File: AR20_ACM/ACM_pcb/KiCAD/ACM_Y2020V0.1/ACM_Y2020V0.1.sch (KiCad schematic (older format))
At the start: 2 parts, among them J1 TC2030-MCP-NL, U1 ATmega328PB-AU

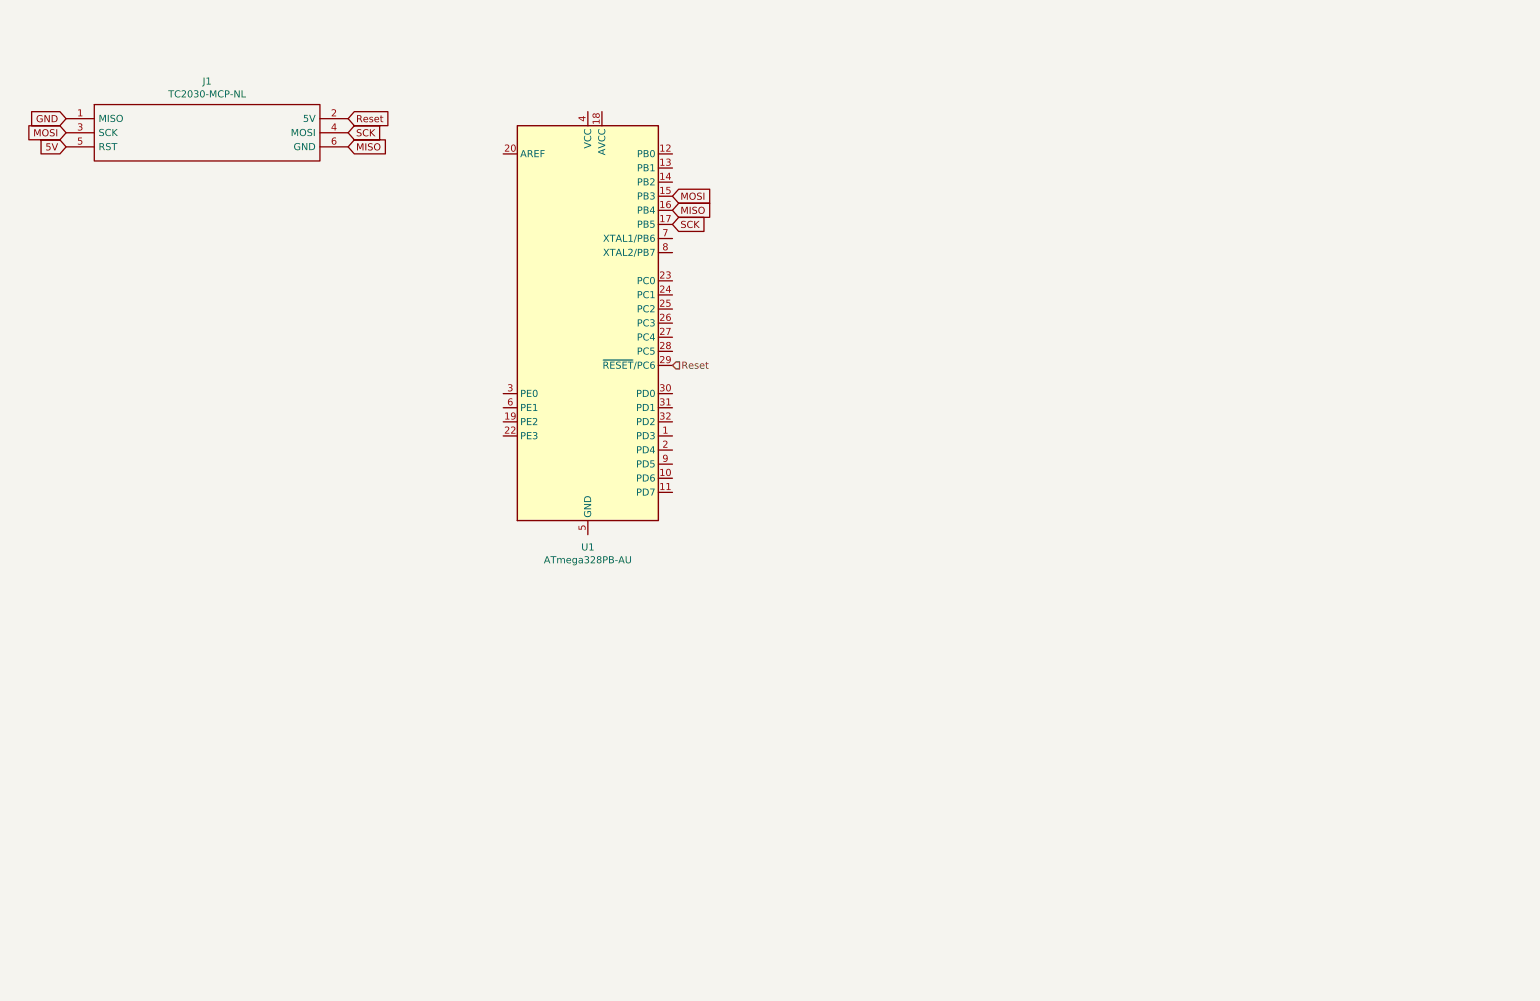
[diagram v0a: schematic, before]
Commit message: Added MCP25625 and PDFS
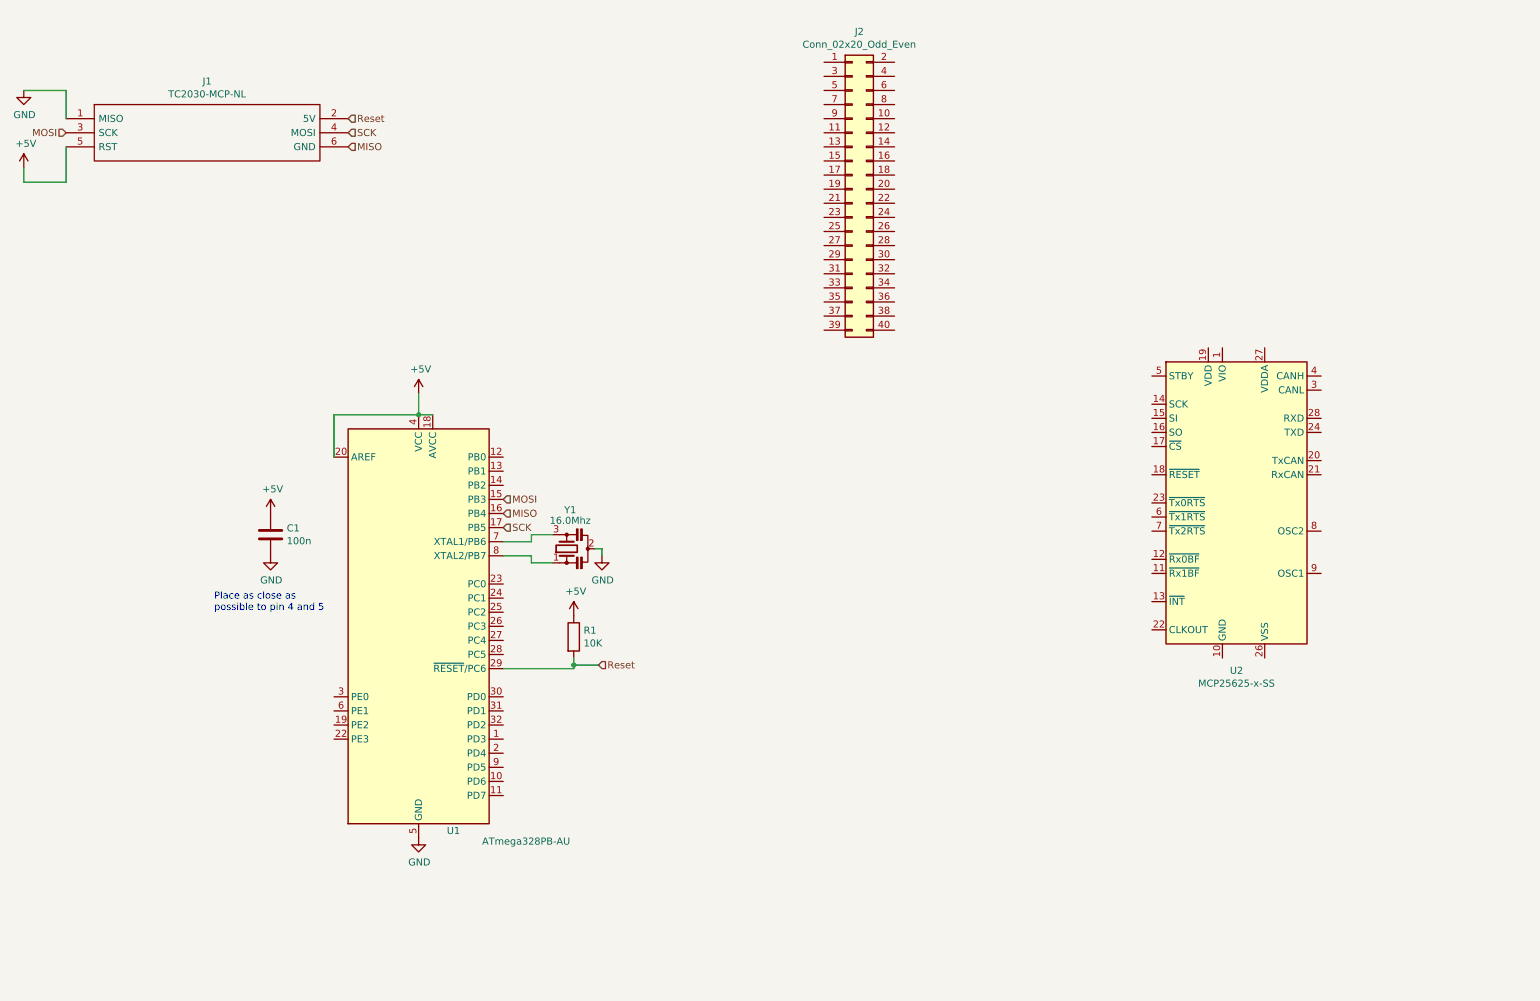
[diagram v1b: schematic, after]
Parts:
- added C1: 100n, Capacitor_SMD:C_0402_1005Metric, symbol Device:C
- added J2: Conn_02x20_Odd_Even, Connector_PinSocket_1.00mm:PinSocket_2x20_P1.00mm_Vertical_SMD, symbol Connector_Generic:Conn_02x20_Odd_Even
- added R1: 10K, Resistor_SMD:R_0402_1005Metric, symbol Device:R
- added U2: MCP25625-x-SS, Package_DFN_QFN:QFN-28-1EP_6x6mm_P0.65mm_EP4.8x4.8mm, symbol Interface_CAN_LIN:MCP25625-x-SS
- added Y1: 16.0Mhz, CSTNE16M0V530000R0:CSTNE16M0V530000R0, symbol Device:Resonator_Small
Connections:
- net 5V is gone; now on net +5V: J1.5 (RST)
- net GND: now also U1.21 (GND), U1.5 (GND), C1.2, Y1.2
- net Reset: now also R1.2
- net +5V: now reaches U1.18 (AVCC)
- net +5V: now also U1.20 (AREF), U1.4 (VCC), C1.1, R1.1
- net at U1.7 (XTAL1/PB6): now also Y1.3
- net at U1.8 (XTAL2/PB7): now also Y1.1
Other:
- note added: "Place as close as \npossible to pin 4 and 5"
- moved on the sheet: U1
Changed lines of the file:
@@
 EESchema Schematic File Version 4
+LIBS:ACM_Y2020V0.1-cache
 EELAYER 29 0
 EELAYER END
@@
 	1    0    0    -1
 $EndComp
+Text HLabel 3950 4250 2    50   Input ~ 0
+SCK
+Text HLabel 3950 4150 2    50   Input ~ 0
+MISO
+Text HLabel 3950 4050 2    50   Input ~ 0
+MOSI
+Text HLabel 850  1450 0    50   Input ~ 0
+MOSI
+Text HLabel 2850 1350 2    50   Input ~ 0
+Reset
+Text HLabel 2850 1450 2    50   Input ~ 0
+SCK
+Text HLabel 2850 1550 2    50   Input ~ 0
+MISO
+$Comp
+L power:GND #PWR0101
+U 1 1 5D3A6728
+P 550 1150
+F 0 "#PWR0101" H 550 900 50  0001 C CNN
+F 1 "GND" H 555 977 50  0000 C CNN
+F 2 "" H 550 1150 50  0001 C CNN
+F 3 "" H 550 1150 50  0001 C CNN
+	1    550  1150
+	1    0    0    -1
+$EndComp
+$Comp
+L power:GND #PWR0102
+U 1 1 5D3A8A7B
+P 3350 6450
+F 0 "#PWR0102" H 3350 6200 50  0001 C CNN
+F 1 "GND" H 3355 6277 50  0000 C CNN
+F 2 "" H 3350 6450 50  0001 C CNN
+F 3 "" H 3350 6450 50  0001 C CNN
+	1    3350 6450
+	1    0    0    -1
+$EndComp
+Wire Wire Line
+	850  1350 850  1150
+Wire Wire Line
+	850  1150 550  1150
+Wire Wire Line
+	850  1550 850  1800
+Wire Wire Line
+	850  1800 550  1800
+Wire Wire Line
+	550  1800 550  1700
+$Comp
+L power:+5V #PWR0103
+U 1 1 5D3A42C5
+P 550 1700
+F 0 "#PWR0103" H 550 1550 50  0001 C CNN
+F 1 "+5V" H 565 1873 50  0000 C CNN
+F 2 "" H 550 1700 50  0001 C CNN
+F 3 "" H 550 1700 50  0001 C CNN
+	1    550  1700
+	1    0    0    -1
+$EndComp
+$Comp
+L power:+5V #PWR0104
+U 1 1 5D3AF650
+P 3350 3300
+F 0 "#PWR0104" H 3350 3150 50  0001 C CNN
+F 1 "+5V" H 3365 3473 50  0000 C CNN
+F 2 "" H 3350 3300 50  0001 C CNN
+F 3 "" H 3350 3300 50  0001 C CNN
+	1    3350 3300
+	1    0    0    -1
+$EndComp
+Wire Wire Line
+	3450 3450 3350 3450
+Wire Wire Line
+	3350 3300 3350 3450
+Connection ~ 3350 3450
+Wire Wire Line
+	2750 3750 2750 3450
+Wire Wire Line
+	2750 3450 3350 3450
+$Comp
+L Device:C C1
+U 1 1 5D3B17F8
+P 2300 4300
+F 0 "C1" H 2415 4346 50  0000 L CNN
+F 1 "100n" H 2415 4255 50  0000 L CNN
+F 2 "Capacitor_SMD:C_0402_1005Metric" H 2338 4150 50  0001 C CNN
+F 3 "~" H 2300 4300 50  0001 C CNN
+	1    2300 4300
+	1    0    0    -1
+$EndComp
+$Comp
+L power:+5V #PWR0105
+U 1 1 5D3B309C
+P 2300 4150
+F 0 "#PWR0105" H 2300 4000 50  0001 C CNN
+F 1 "+5V" H 2315 4323 50  0000 C CNN
+F 2 "" H 2300 4150 50  0001 C CNN
+F 3 "" H 2300 4150 50  0001 C CNN
+	1    2300 4150
+	1    0    0    -1
+$EndComp
+$Comp
+L power:GND #PWR0106
+U 1 1 5D3B39A1
+P 2300 4450
+F 0 "#PWR0106" H 2300 4200 50  0001 C CNN
+F 1 "GND" H 2305 4277 50  0000 C CNN
+F 2 "" H 2300 4450 50  0001 C CNN
+F 3 "" H 2300 4450 50  0001 C CNN
+	1    2300 4450
+	1    0    0    -1
+$EndComp
+Text Notes 1900 4850 0    50   ~ 0
+Place as close as \npossible to pin 4 and 5
+$Comp
+L Device:Resonator_Small Y1
+U 1 1 5D3C125F
+P 4400 4400
+F 0 "Y1" V 4675 4375 50  0000 C CNN
+F 1 "16.0Mhz" V 4600 4375 50  0000 C CNN
+F 2 "CSTNE16M0V530000R0:CSTNE16M0V530000R0" H 4375 4400 50  0001 C CNN
+F 3 "~" H 4375 4400 50  0001 C CNN
+	1    4400 4400
+	0    -1   -1   0
+$EndComp
+$Comp
+L power:GND #PWR0107
+U 1 1 5D3C307D
+P 4650 4450
+F 0 "#PWR0107" H 4650 4200 50  0001 C CNN
+F 1 "GND" H 4655 4277 50  0000 C CNN
+F 2 "" H 4650 4450 50  0001 C CNN
+F 3 "" H 4650 4450 50  0001 C CNN
+	1    4650 4450
+	1    0    0    -1
+$EndComp
+Wire Wire Line
+	3950 4450 4150 4450
+Wire Wire Line
+	4150 4450 4150 4500
+Wire Wire Line
+	4150 4500 4300 4500
+Wire Wire Line
+	3950 4350 4150 4350
+Wire Wire Line
+	4150 4350 4150 4300
+Wire Wire Line
+	4150 4300 4300 4300
+Wire Wire Line
+	4600 4400 4650 4400
+Wire Wire Line
+	4650 4400 4650 4450
+$Comp
+L Device:R R1
+U 1 1 5D3CAE32
+P 4450 5025
+F 0 "R1" H 4520 5071 50  0000 L CNN
+F 1 "10K" H 4520 4980 50  0000 L CNN
+F 2 "Resistor_SMD:R_0402_1005Metric" V 4380 5025 50  0001 C CNN
+F 3 "~" H 4450 5025 50  0001 C CNN
+	1    4450 5025
+	1    0    0    -1
+$EndComp
+Wire Wire Line
+	3950 5250 4450 5250
+$Comp
+L power:+5V #PWR0108
+U 1 1 5D3CE356
+P 4450 4875
+F 0 "#PWR0108" H 4450 4725 50  0001 C CNN
+F 1 "+5V" H 4465 5048 50  0000 C CNN
+F 2 "" H 4450 4875 50  0001 C CNN
+F 3 "" H 4450 4875 50  0001 C CNN
+	1    4450 4875
+	1    0    0    -1
+$EndComp
+Connection ~ 4450 5225
+Wire Wire Line
+	4450 5225 4450 5175
+Wire Wire Line
+	4450 5250 4450 5225
+Wire Wire Line
+	4625 5225 4450 5225
+Text HLabel 4625 5225 2    50   Input ~ 0
+Reset
 $Comp
 L MCU_Microchip_ATmega:ATmega328PB-AU U1
 U 1 1 5D38D7A6
-P 4550 2800
-F 0 "U1" H 4550 1211 50  0000 C CNN
-F 1 "ATmega328PB-AU" H 4550 1120 50  0000 C CNN
-F 2 "Package_QFP:TQFP-32_7x7mm_P0.8mm" H 4550 2800 50  0001 C CIN
-F 3 "http://ww1.microchip.com/downloads/en/DeviceDoc/40001906C.pdf" H 4550 2800 50  0001 C CNN
-	1    4550 2800
-	1    0    0    -1
-$EndComp
-Text GLabel 2850 1350 2    50   Input ~ 0
-Reset
-Text GLabel 2850 1450 2    50   Input ~ 0
-SCK
-Text GLabel 2850 1550 2    50   Input ~ 0
-MISO
-Text GLabel 850  1350 0    50   Input ~ 0
-GND
-Text GLabel 850  1450 0    50   Input ~ 0
-MOSI
-Text GLabel 850  1550 0    50   Input ~ 0
-5V
-Text GLabel 5150 1900 2    50   Input ~ 0
-MOSI
-Text GLabel 5150 2000 2    50   Input ~ 0
-MISO
-Text GLabel 5150 2100 2    50   Input ~ 0
-SCK
-Text HLabel 5150 3100 2    50   Input ~ 0
-Reset
+P 3350 4950
+F 0 "U1" H 3550 3500 50  0000 L CNN
+F 1 "ATmega328PB-AU" H 3800 3425 50  0000 L CNN
+F 2 "Package_QFP:TQFP-32_7x7mm_P0.8mm" H 3350 4950 50  0001 C CIN
+F 3 "http://ww1.microchip.com/downloads/en/DeviceDoc/40001906C.pdf" H 3350 4950 50  0001 C CNN
+	1    3350 4950
+	1    0    0    -1
+$EndComp
+$Comp
+L Interface_CAN_LIN:MCP25625-x-SS U2
+U 1 1 5D3DCB03
+P 9150 4075
+F 0 "U2" H 9150 2886 50  0000 C CNN
+F 1 "MCP25625-x-SS" H 9150 2795 50  0000 C CNN
+F 2 "Package_DFN_QFN:QFN-28-1EP_6x6mm_P0.65mm_EP4.8x4.8mm" H 9250 3775 50  0001 C CNN
+F 3 "http://ww1.microchip.com/downloads/en/DeviceDoc/20005282B.pdf" H 9150 4675 50  0001 C CNN
+	1    9150 4075
+	1    0    0    -1
+$EndComp
+$Comp
+L Connector_Generic:Conn_02x20_Odd_Even J2
+U 1 1 5D3E347E
+P 6425 1850
+F 0 "J2" H 6475 2967 50  0000 C CNN
+F 1 "Conn_02x20_Odd_Even" H 6475 2876 50  0000 C CNN
+F 2 "Connector_PinSocket_1.00mm:PinSocket_2x20_P1.00mm_Vertical_SMD" H 6425 1850 50  0001 C CNN
+F 3 "~" H 6425 1850 50  0001 C CNN
+	1    6425 1850
+	1    0    0    -1
+$EndComp
 $EndSCHEMATC

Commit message: See change log for update.
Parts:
- added C2, C3, C4, C5: 0.1uF, Capacitor_SMD:C_0402_1005Metric, symbol Device:C
- added D1: 15V, Diode_SMD:D_SOD-323F, symbol Device:D_Zener
- added F1: 200mA, Fuse:Fuse_0603_1608Metric, symbol Device:Polyfuse_Small
- added R2: 120Ohm, Resistor_SMD:R_0603_1608Metric, symbol Device:R
- added R3: 10KOhm, Resistor_SMD:R_0402_1005Metric, symbol Device:R
- added U3: SPX3819M5-L-5-0, Package_TO_SOT_SMD:SOT-23-5, symbol Regulator_Linear:SPX3819M5-L-5-0
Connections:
- net labels added: +12V, CANH, CANL, CAN_CS, CAN_INT, CLK_MCP
- wire segments 21 -> 64
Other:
- note added: "CAN MCU"
- note added: "Close as possible to MCP-chip"
- note added: "Connector"
- note added: "ICSP"
- note added: "Main MCU"
- note added: "Power and protection circuits"
- moved on the sheet: C1, J1, J2, R1, U1, U2, Y1

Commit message: Changelog for 27.07.2019
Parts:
- removed J2: Conn_02x20_Odd_Even, Connector_PinSocket_1.00mm:PinSocket_2x20_P1.00mm_Vertical_SMD, symbol Connector_Generic:Conn_02x20_Odd_Even
- added D2: D_Small, Diode_SMD:D_0402_1005Metric, symbol Device:D_Small
- added J2: Conn_02x15_Odd_Even, Connector_PinSocket_0.8mm:PinSocket_2x15_P0.08mm_Vertical_SMD, symbol Connector_Generic:Conn_02x15_Odd_Even
- added LED1: SMLP36RGB2W3R, SMLP36RGB2W3R:SMLP36RGB2W3R, symbol SMLP36RGB2W3R:SMLP36RGB2W3R
- added R4: 200 Ohm, Resistor_SMD:R_0402_1005Metric, symbol Device:R
- added R5: 290 Ohm, Resistor_SMD:R_0402_1005Metric, symbol Device:R
- added R6: 190 Ohm, Resistor_SMD:R_0402_1005Metric, symbol Device:R
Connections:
- net labels added: BLUE_LED, GREEN_LED, RED_LED, U-Pin10, U-Pin12, U-Pin14, U-Pin16, U-Pin18, U-Pin20, U-Pin22, U-Pin24, U-Pin26, U-Pin28, U-Pin8
- wire segments 64 -> 89
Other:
- note added: "Diode for reverse\npolarity protection"
- note added: "LED Circuit"
- note added: "Legg ut RESET for Debugwire"
- note added: "Polyfuse for\novercurrent protection"
- note added: "Zener diode for\novervoltage protection"
- moved on the sheet: J1

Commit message: Changelog for 28.07.2019
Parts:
- removed D2: D_Small, Diode_SMD:D_0402_1005Metric, symbol Device:D_Small
- added D2: 2.4V, Diode_SMD:D_SOD-523, symbol Device:D_Zener
- added Q1: Q_PMOS_DGS, Package_TO_SOT_SMD:SOT-23, symbol Device:Q_PMOS_GSD
- added R7: 100K Ohm, Resistor_SMD:R_0402_1005Metric, symbol Device:R
- D1: footprint Diode_SMD:D_SOD-323F -> Diode_SMD:D_SOD-523; Farnell (none) -> https://no.farnell.com/nexperia/bzx585-c15-115/diode-zener-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
- F1: value 200mA -> 250mA; Farnell (none) -> https://no.farnell.com/bel-fuse-circuit-protection/0zcm0010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
- J2: RS (none) -> https://no.rs-online.com/web/p/pcb-sockets/0437152/
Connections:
- net CANH is gone; now on net U-Pin27: R2.1, U2.4 (CANH)
- net CANL is gone; now on net U-Pin29: R2.2, U2.3 (CANL)
- net +12V: no longer D1.1 (K)
- net +5V: no longer J2.5 (Pin_5)
- net BLUE_LED: now also J2.19 (Pin_19)
- net CLK_MCP: now also U2.9 (OSC1)
- net GND: now also J2.16 (Pin_16), J2.18 (Pin_18), U2.5 (STBY), R7.2; no longer J2.2 (Pin_2), J2.4 (Pin_4), J2.6 (Pin_6)
- net RED_LED: now also J2.21 (Pin_21)
- net Reset: now also J2.10 (Pin_10)
- net U-Pin12: now also U1.30 (PD0); no longer U1.23 (PC0)
- net U-Pin14: now also U1.31 (PD1); no longer U1.24 (PC1)
- net U-Pin20: now also U1.1 (PD3); no longer U1.27 (PC4)
- net U-Pin22: now also U1.2 (PD4); no longer U1.28 (PC5)
- net U-Pin24: now also U1.3 (PE0); no longer U1.30 (PD0)
- net U-Pin26: no longer J2.26 (Pin_26), U1.31 (PD1)
- net U-Pin28: no longer J2.28 (Pin_28)
- net U-Pin8: now also U1.28 (PC5); no longer U1.19 (PE2)
- net U-Pin23: now reaches U1.10 (PD6)
- net U-Pin23: now also J2.23 (Pin_23)
- net U-Pin30: now reaches U1.6 (PE1)
- net U-Pin30: now also J2.30 (Pin_30)
- net at U3.1 (IN): now also D2.1 (K), Q1.2 (S); no longer F1.1
- net U-Pin11: now reaches J2.11 (Pin_11)
- net U-Pin11: now also U1.19 (PE2)
- net U-Pin13: now reaches J2.13 (Pin_13)
- net U-Pin15: now reaches J2.15 (Pin_15)
- net U-Pin17: now reaches J2.17 (Pin_17)
- net U-Pin25: now reaches J2.25 (Pin_25)
- net U-Pin27: now reaches J2.27 (Pin_27)
- net U-Pin29: now reaches J2.29 (Pin_29)
- net U-Pin7: now reaches J2.7 (Pin_7)
- net U-Pin7: now also U1.23 (PC0)
- net U-Pin9: now reaches J2.9 (Pin_9)
- net U-Pin9: now also U1.22 (PE3)
- removed net U-Pin10: J2.10 (Pin_10), U1.22 (PE3)
- net U-Pin16 renamed U-Pin2
- net U-Pin2: now also J2.2 (Pin_2); no longer J2.16 (Pin_16)
- net U-Pin18 renamed U-Pin4
- net U-Pin4: now also J2.4 (Pin_4); no longer J2.18 (Pin_18)
- new net: D1.1 (K), F1.1, Q1.3 (D)
- new net: D2.2 (A), Q1.1 (G), R7.1
- new net U-Pin5: J2.5 (Pin_5), U1.24 (PC1)
- new net U-Pin6: J2.6 (Pin_6), U1.27 (PC4)
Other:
- note added: "NB! Vgs max: ±10V!\n2.4V zener diode\nfor Vgs -2.4V"
- note added: "P-mosfet for reverse\npolarity protection"
- note added: "Trenger flere Decupling Caps?"
- note removed: "Diode for reverse\npolarity protection"
- moved on the sheet: D1, F1, U3
